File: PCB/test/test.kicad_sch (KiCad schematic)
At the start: 56 parts, among them CN3 USB_1, CN4 HEADER_1X4, CN5 UFL, SW2 MLL1200S_TE, U1 STM32WBxx_QFN48, U2 USBLC6-2SC6, U3 LD3985M33R, X1 NX2016_32MHz, X2 NX2012_32K768Hz

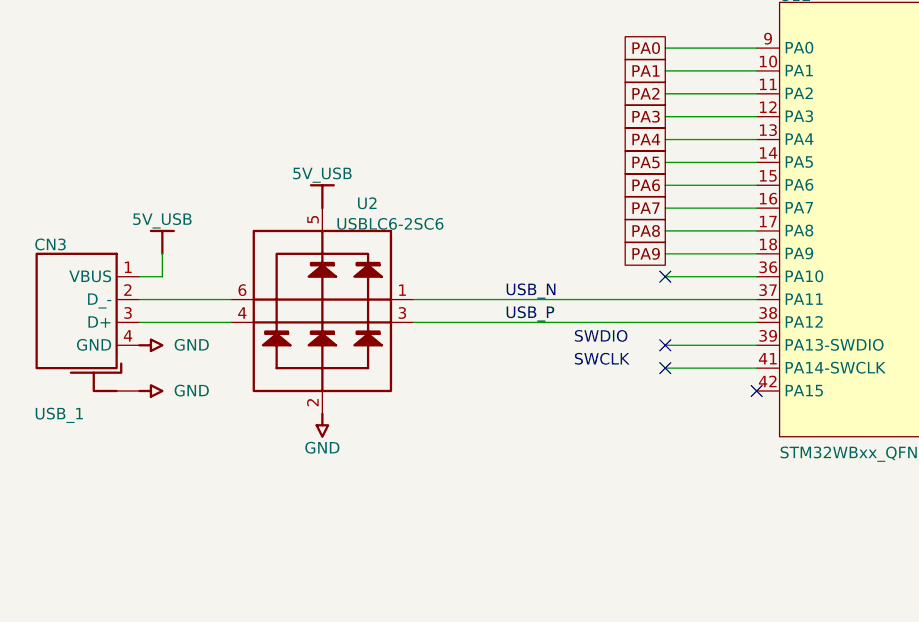
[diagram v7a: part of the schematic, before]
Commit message: ajout usb
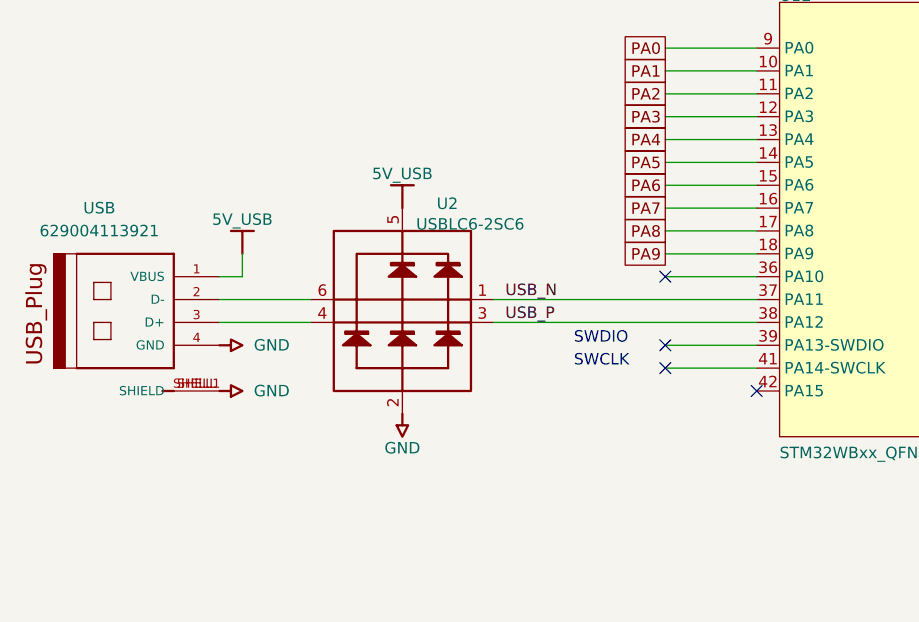
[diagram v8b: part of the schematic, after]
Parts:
- removed CN3: USB_1, USB_A_M1, symbol test-altium-import:0_USB_1
- added USB: 629004113921, 629004113921, symbol 629004113921:629004113921
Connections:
- net 5V_USB: now also USB.1 (VBUS)
- net GND: now also USB.4 (GND), USB.SHELL (SHIELD), USB.SHELL1 (SHIELD)
- net at U2.4: now also USB.3 (D+)
- net at U2.6: now also USB.2 (D-)
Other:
- moved on the sheet: U2
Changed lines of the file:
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@@
     (stroke (width 0.254) (type default) (color 0 0 0 0))
   )
-  (wire (pts (xy 24.13 43.18) (xy 13.97 43.18))
+  (wire (pts (xy 33.02 43.18) (xy 22.86 43.18))
     (stroke (width 0.254) (type default) (color 0 0 0 0))
   )
@@
     (stroke (width 0) (type solid) (color 0 0 0 0))
   )
-  (wire (pts (xy 16.51 35.56) (xy 16.51 38.1))
+  (wire (pts (xy 25.4 35.56) (xy 25.4 38.1))
     (stroke (width 0.254) (type default) (color 0 0 0 0))
   )
@@
     (stroke (width 0.254) (type default) (color 0 0 0 0))
   )
-  (wire (pts (xy 16.51 38.1) (xy 13.97 38.1))
+  (wire (pts (xy 25.4 38.1) (xy 22.86 38.1))
     (stroke (width 0.254) (type default) (color 0 0 0 0))
   )
@@
     (stroke (width 0.254) (type default) (color 0 0 0 0))
   )
-  (wire (pts (xy 44.45 43.18) (xy 82.55 43.18))
+  (wire (pts (xy 53.34 43.18) (xy 82.55 43.18))
     (stroke (width 0.254) (type default) (color 0 0 0 0))
   )
@@
     (stroke (width 0.254) (type default) (color 0 0 0 0))
   )
-  (wire (pts (xy 44.45 40.64) (xy 82.55 40.64))
+  (wire (pts (xy 53.34 40.64) (xy 82.55 40.64))
     (stroke (width 0.254) (type default) (color 0 0 0 0))
   )
@@
     (stroke (width 0.254) (type default) (color 0 0 0 0))
   )
-  (wire (pts (xy 13.97 40.64) (xy 24.13 40.64))
+  (wire (pts (xy 22.86 40.64) (xy 33.02 40.64))
     (stroke (width 0.254) (type default) (color 0 0 0 0))
   )
@@
     (pin "")
   )
-  (symbol (lib_id "test-altium-import:GND") (at 13.97 45.72 90) (unit 1)
+  (symbol (lib_id "test-altium-import:GND") (at 22.86 45.72 90) (unit 1)
     (in_bom yes) (on_board yes)
-    (property "Reference" "#PWR0135" (id 0) (at 13.97 45.72 0)
+    (property "Reference" "#PWR0135" (id 0) (at 22.86 45.72 0)
       (effects (font (size 1.27 1.27)) hide)
     )
-    (property "Value" "GND" (id 1) (at 17.78 45.72 90)
+    (property "Value" "GND" (id 1) (at 26.67 45.72 90)
       (effects (font (size 1.27 1.27)) (justify right))
     )
-    (property "Footprint" "" (id 2) (at 13.97 45.72 0)
+    (property "Footprint" "" (id 2) (at 22.86 45.72 0)
       (effects (font (size 1.27 1.27)) hide)
     )
-    (property "Datasheet" "" (id 3) (at 13.97 45.72 0)
+    (property "Datasheet" "" (id 3) (at 22.86 45.72 0)
       (effects (font (size 1.27 1.27)) hide)
     )
@@
     (pin "2")
   )
-  (symbol (lib_id "test-altium-import:GND") (at 13.97 50.8 90) (unit 1)
+  (symbol (lib_id "test-altium-import:GND") (at 22.86 50.8 90) (unit 1)
     (in_bom yes) (on_board yes)
-    (property "Reference" "#PWR0137" (id 0) (at 13.97 50.8 0)
+    (property "Reference" "#PWR0137" (id 0) (at 22.86 50.8 0)
       (effects (font (size 1.27 1.27)) hide)
     )
-    (property "Value" "GND" (id 1) (at 17.78 50.8 90)
+    (property "Value" "GND" (id 1) (at 26.67 50.8 90)
       (effects (font (size 1.27 1.27)) (justify right))
     )
-    (property "Footprint" "" (id 2) (at 13.97 50.8 0)
+    (property "Footprint" "" (id 2) (at 22.86 50.8 0)
       (effects (font (size 1.27 1.27)) hide)
     )
-    (property "Datasheet" "" (id 3) (at 13.97 50.8 0)
+    (property "Datasheet" "" (id 3) (at 22.86 50.8 0)
       (effects (font (size 1.27 1.27)) hide)
     )
@@
     (pin "9")
   )
-  (symbol (lib_id "test-altium-import:0_mirrored_USBLC6-2") (at 41.91 38.1 0) (unit 1)
+  (symbol (lib_id "test-altium-import:0_mirrored_USBLC6-2") (at 50.8 38.1 0) (unit 1)
     (in_bom yes) (on_board yes)
-    (property "Reference" "U2" (id 0) (at 38.1 30.734 0)
+    (property "Reference" "U2" (id 0) (at 46.99 30.734 0)
       (effects (font (size 1.27 1.27)) (justify left bottom))
     )
-    (property "Value" "USBLC6-2SC6" (id 1) (at 35.814 33.02 0)
+    (property "Value" "USBLC6-2SC6" (id 1) (at 44.704 33.02 0)
       (effects (font (size 1.27 1.27)) (justify left bottom))
     )
-    (property "Footprint" "SOT23-6" (id 2) (at 41.91 38.1 0)
+    (property "Footprint" "SOT23-6" (id 2) (at 50.8 38.1 0)
       (effects (font (size 1.27 1.27)) hide)
     )
-    (property "Datasheet" "" (id 3) (at 41.91 38.1 0)
+    (property "Datasheet" "" (id 3) (at 50.8 38.1 0)
       (effects (font (size 1.27 1.27)) hide)
     )
@@
     (pin "2")
   )
-  (symbol (lib_id "test-altium-import:GND") (at 34.29 53.34 0) (unit 1)
+  (symbol (lib_id "test-altium-import:GND") (at 43.18 53.34 0) (unit 1)
     (in_bom yes) (on_board yes)
-    (property "Reference" "#PWR0134" (id 0) (at 34.29 53.34 0)
+    (property "Reference" "#PWR0134" (id 0) (at 43.18 53.34 0)
       (effects (font (size 1.27 1.27)) hide)
     )
-    (property "Value" "GND" (id 1) (at 34.29 57.15 0))
-    (property "Footprint" "" (id 2) (at 34.29 53.34 0)
+    (property "Value" "GND" (id 1) (at 43.18 57.15 0))
+    (property "Footprint" "" (id 2) (at 43.18 53.34 0)
       (effects (font (size 1.27 1.27)) hide)
     )
-    (property "Datasheet" "" (id 3) (at 34.29 53.34 0)
+    (property "Datasheet" "" (id 3) (at 43.18 53.34 0)
       (effects (font (size 1.27 1.27)) hide)
     )
@@
     (pin "")
   )
-  (symbol (lib_id "test-altium-import:5V_USB") (at 16.51 35.56 180) (unit 1)
+  (symbol (lib_id "629004113921:629004113921") (at 15.24 43.18 0) (mirror y) (unit 1)
+    (in_bom yes) (on_board yes) (fields_autoplaced)
+    (property "Reference" "USB" (id 0) (at 9.5051 30.48 0))
+    (property "Value" "629004113921" (id 1) (at 9.5051 33.02 0))
+    (property "Footprint" "629004113921" (id 2) (at 15.24 43.18 0)
+      (effects (font (size 1.27 1.27)) (justify left bottom) hide)
+    )
+    (property "Datasheet" "" (id 3) (at 15.24 43.18 0)
+      (effects (font (size 1.27 1.27)) (justify left bottom) hide)
+    )
+    (pin "1")
+    (pin "2")
+    (pin "3")
+    (pin "4")
+    (pin "SHELL")
+    (pin "SHELL1")
+  )
+  (symbol (lib_id "test-altium-import:5V_USB") (at 25.4 35.56 180) (unit 1)
     (in_bom yes) (on_board yes)
-    (property "Reference" "#PWR0136" (id 0) (at 16.51 35.56 0)
+    (property "Reference" "#PWR0136" (id 0) (at 25.4 35.56 0)
       (effects (font (size 1.27 1.27)) hide)
     )
-    (property "Value" "5V_USB" (id 1) (at 16.51 31.75 0))
-    (property "Footprint" "" (id 2) (at 16.51 35.56 0)
+    (property "Value" "5V_USB" (id 1) (at 25.4 31.75 0))
+    (property "Footprint" "" (id 2) (at 25.4 35.56 0)
       (effects (font (size 1.27 1.27)) hide)
     )
-    (property "Datasheet" "" (id 3) (at 16.51 35.56 0)
+    (property "Datasheet" "" (id 3) (at 25.4 35.56 0)
       (effects (font (size 1.27 1.27)) hide)
     )
@@
     (pin "")
   )
-  (symbol (lib_id "test-altium-import:5V_USB") (at 34.29 30.48 180) (unit 1)
+  (symbol (lib_id "test-altium-import:5V_USB") (at 43.18 30.48 180) (unit 1)
     (in_bom yes) (on_board yes)
-    (property "Reference" "#PWR0133" (id 0) (at 34.29 30.48 0)
+    (property "Reference" "#PWR0133" (id 0) (at 43.18 30.48 0)
       (effects (font (size 1.27 1.27)) hide)
     )
-    (property "Value" "5V_USB" (id 1) (at 34.29 26.67 0))
-    (property "Footprint" "" (id 2) (at 34.29 30.48 0)
+    (property "Value" "5V_USB" (id 1) (at 43.18 26.67 0))
+    (property "Footprint" "" (id 2) (at 43.18 30.48 0)
       (effects (font (size 1.27 1.27)) hide)
     )
-    (property "Datasheet" "" (id 3) (at 34.29 30.48 0)
+    (property "Datasheet" "" (id 3) (at 43.18 30.48 0)
       (effects (font (size 1.27 1.27)) hide)
     )
@@
     (pin "")
   )
-  (symbol (lib_id "test-altium-import:0_USB_1") (at 11.43 43.18 0) (unit 1)
-    (in_bom yes) (on_board yes)
-    (property "Reference" "CN3" (id 0) (at 2.286 35.306 0)
-      (effects (font (size 1.27 1.27)) (justify left bottom))
-    )
-    (property "Value" "USB_1" (id 1) (at 2.286 54.102 0)
-      (effects (font (size 1.27 1.27)) (justify left bottom))
-    )
-    (property "Footprint" "USB_A_M1" (id 2) (at 11.43 43.18 0)
-      (effects (font (size 1.27 1.27)) hide)
-    )
-    (property "Datasheet" "" (id 3) (at 11.43 43.18 0)
-      (effects (font (size 1.27 1.27)) hide)
-    )
-    (pin "0")
-    (pin "1")
-    (pin "2")
-    (pin "3")
-    (pin "4")
-  )
   (symbol (lib_id "power:PWR_FLAG") (at 21.59 190.5 0) (unit 1)
     (in_bom yes) (on_board yes) (fields_autoplaced)
@@
       (reference "C30") (unit 1) (value "0.8pF") (footprint "0402_CAP_NPOL")
     )
-    (path "/f1447ad6-651c-45be-a2d6-33bddf672c2c"
-      (reference "CN3") (unit 1) (value "USB_1") (footprint "USB_A_M1")
-    )
     (path "/12fa3c3f-3d14-451a-a6a8-884fd1b32fa7"
       (reference "CN4") (unit 1) (value "HEADER_1X4") (footprint "SIL4_127_B")
@@
       (reference "U3") (unit 1) (value "LD3985M33R") (footprint "SOT23-5")
     )
+    (path "/a876c6ed-9cd6-4c8f-821d-ad86ce4fa0b8"
+      (reference "USB") (unit 1) (value "629004113921") (footprint "629004113921")
+    )
     (path "/422b10b9-e829-44a2-8808-05edd8cb3050"
